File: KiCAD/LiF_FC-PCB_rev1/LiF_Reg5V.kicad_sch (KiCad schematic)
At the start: 21 parts, among them U3 TPS55285VALR

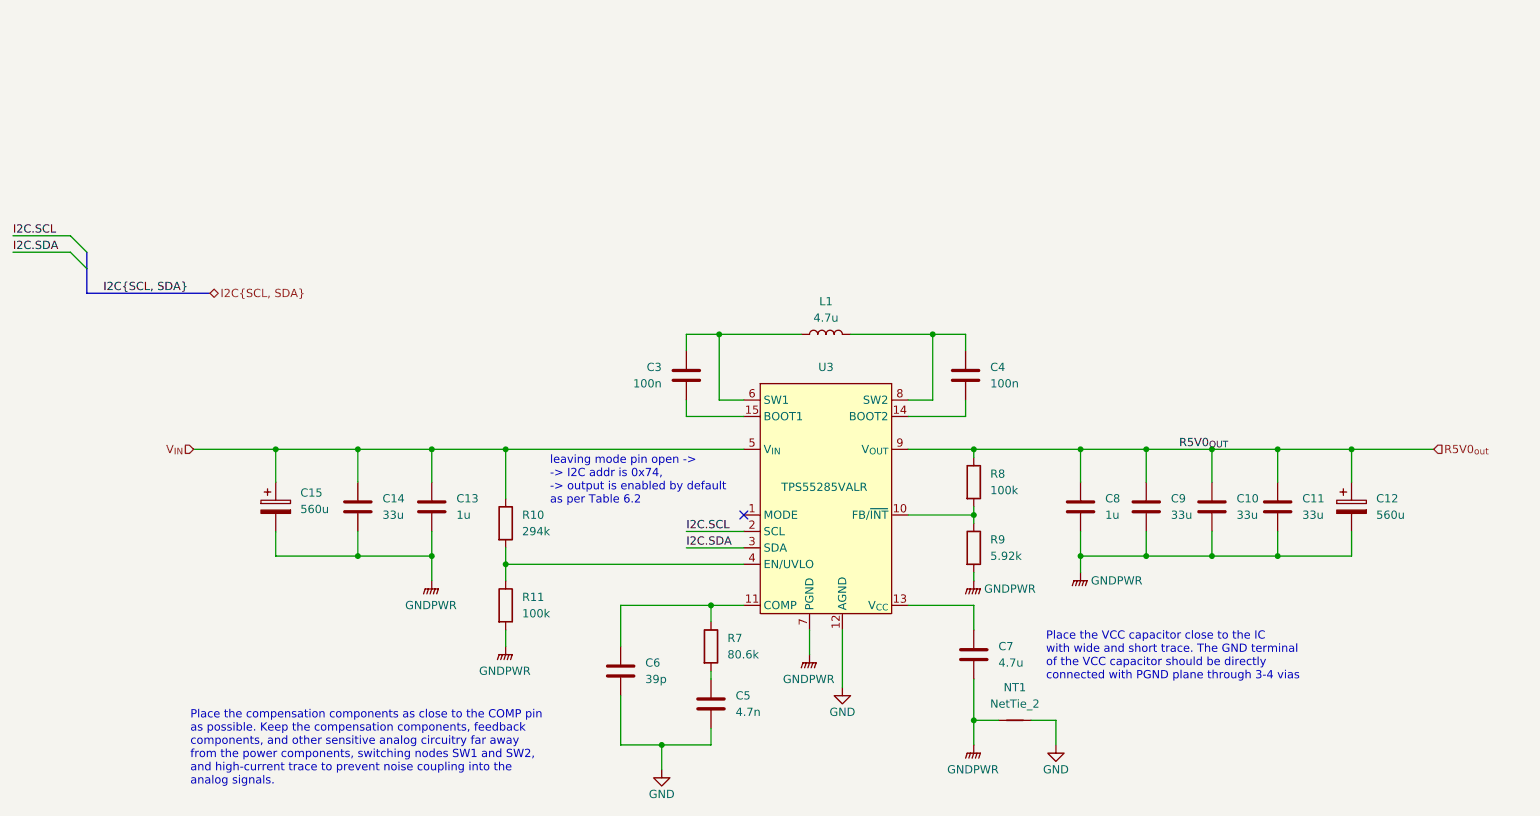
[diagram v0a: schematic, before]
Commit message: reverted 5V reg, reworked power distribution logic, swapped power OR-ing ICs
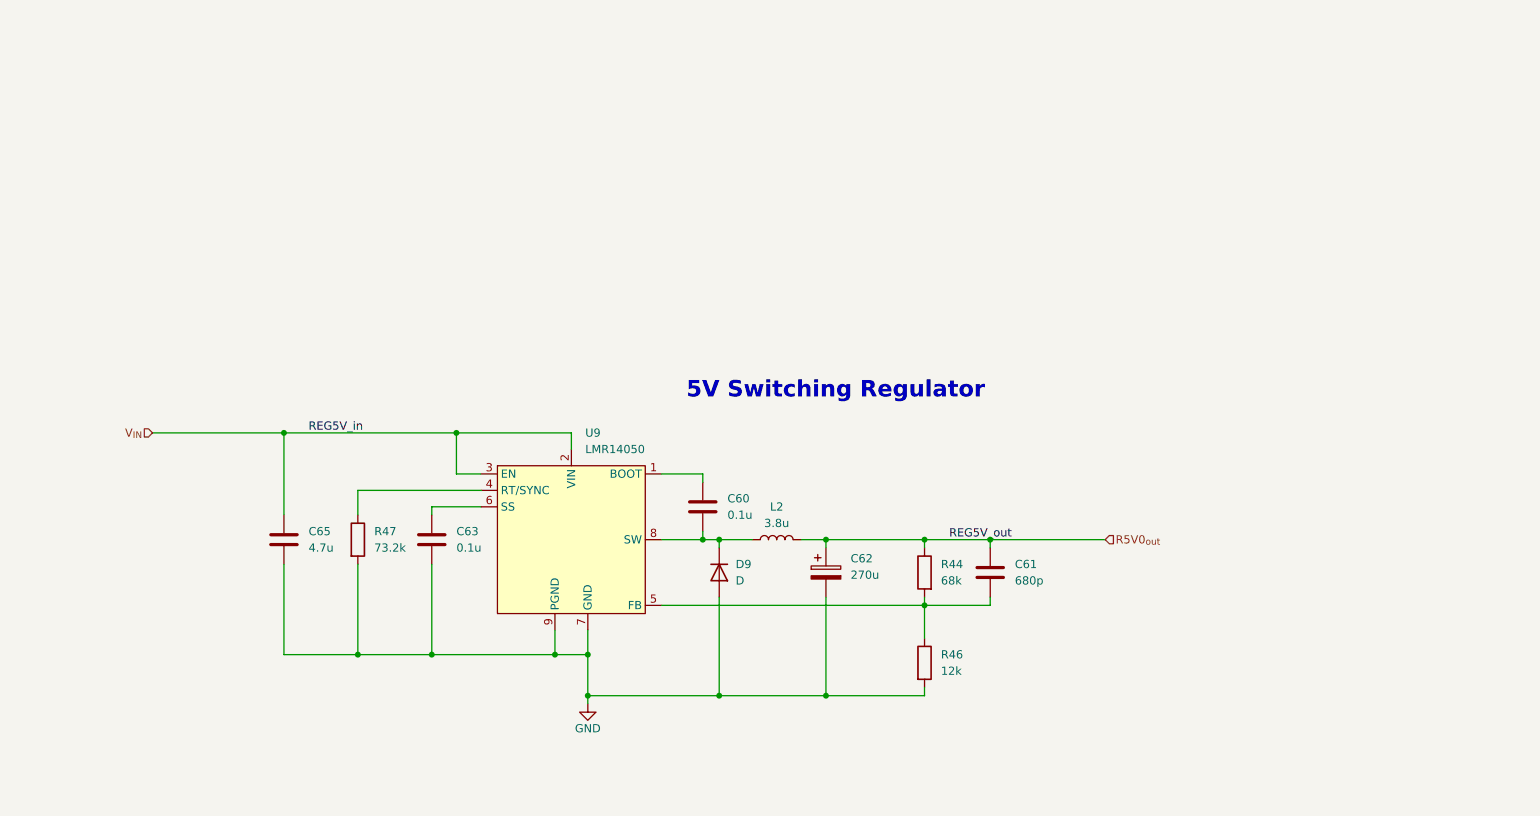
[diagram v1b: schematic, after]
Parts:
- removed C10, C11, C14, C9: 33u, symbol Device:C
- removed C12, C15: 560u, symbol Device:C_Polarized
- removed C13, C8: 1u, symbol Device:C
- removed C3, C4: 100n, symbol Device:C
- removed C5: 4.7n, symbol Device:C
- removed C6: 39p, symbol Device:C
- removed C7: 4.7u, symbol Device:C
- removed L1: 4.7u, LiF_PCB_Footprints:IND_SPM10040T-4R7M, symbol Device:L
- removed NT1: NetTie_2, NetTie:NetTie-2_SMD_Pad0.5mm, symbol Device:NetTie_2
- removed R10: 294k, symbol Device:R
- removed R11, R8: 100k, symbol Device:R
- removed R7: 80.6k, symbol Device:R
- removed R9: 5.92k, symbol Device:R
- removed U3: TPS55285VALR, LiF_PCB_Footprints:WQFN-HR-15, symbol LiF_PCB_Symbols:TPS55285VALR
- added C60, C63: 0.1u, Capacitor_SMD:C_0805_2012Metric, symbol Device:C
- added C61: 680p, Capacitor_SMD:C_0805_2012Metric, symbol Device:C
- added C62: 270u, Capacitor_SMD:CP_Elec_6.3x9.9, symbol Device:C_Polarized
- added C65: 4.7u, Capacitor_SMD:C_0805_2012Metric, symbol Device:C
- added D9: D, Diode_SMD:D_PowerDI-5, symbol Device:D
- added L2: 3.8u, MatsLibrary:IND_BOURNS_SRU1038, symbol Device:L
- added R44: 68k, Resistor_SMD:R_0805_2012Metric, symbol Device:R
- added R46: 12k, Resistor_SMD:R_0805_2012Metric, symbol Device:R
- added R47: 73.2k, Resistor_SMD:R_0805_2012Metric, symbol Device:R
- added U9: LMR14050, Package_SO:Texas_R-PDSO-G8_EP2.95x4.9mm_Mask2.4x3.1mm, symbol LiF_PCB_Symbols:LMR14050SDDAR
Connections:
- net GND: now also C62.2, C63.2, C65.2, D9.2 (A), R46.2, R47.2, U9.7 (GND), U9.9 (PGND)
- net R5V0_{out}: now also C61.1, C62.1, L2.2, R44.1
- net V_{IN}: now also C65.1, U9.2 (VIN), U9.3 (EN)
- new net: C60.2, D9.1 (K), L2.1, U9.8 (SW)
- new net: C60.1, U9.1 (BOOT)
- new net: R47.1, U9.4 (RT/SYNC)
- new net: C61.2, R44.2, R46.1, U9.5 (FB)
- new net: C63.1, U9.6 (SS)
- no-connect marks 1 -> 0
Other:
- note added: "5V Switching Regulator"
- note removed: "Place the VCC capacitor close to the IC with wide and short trace. The GND terminal of the VCC capacitor should be directly connected with PGND plane through 3-4 vias"
- note removed: "Place the compensation components as close to the COMP pin as possible. Keep the compensation components, feedback components, and other sensitive analog circuitry far away from the power components, switching nodes SW1 and SW2, and high-current trace to prevent noise coupling into the analog signals."
- note removed: "leaving mode pin open -> -> I2C addr is 0x74, -> output is enabled by default as per Table 6.2"

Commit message: Finished schematics, mostly. Only MCU sheet left. Doing component sourcing
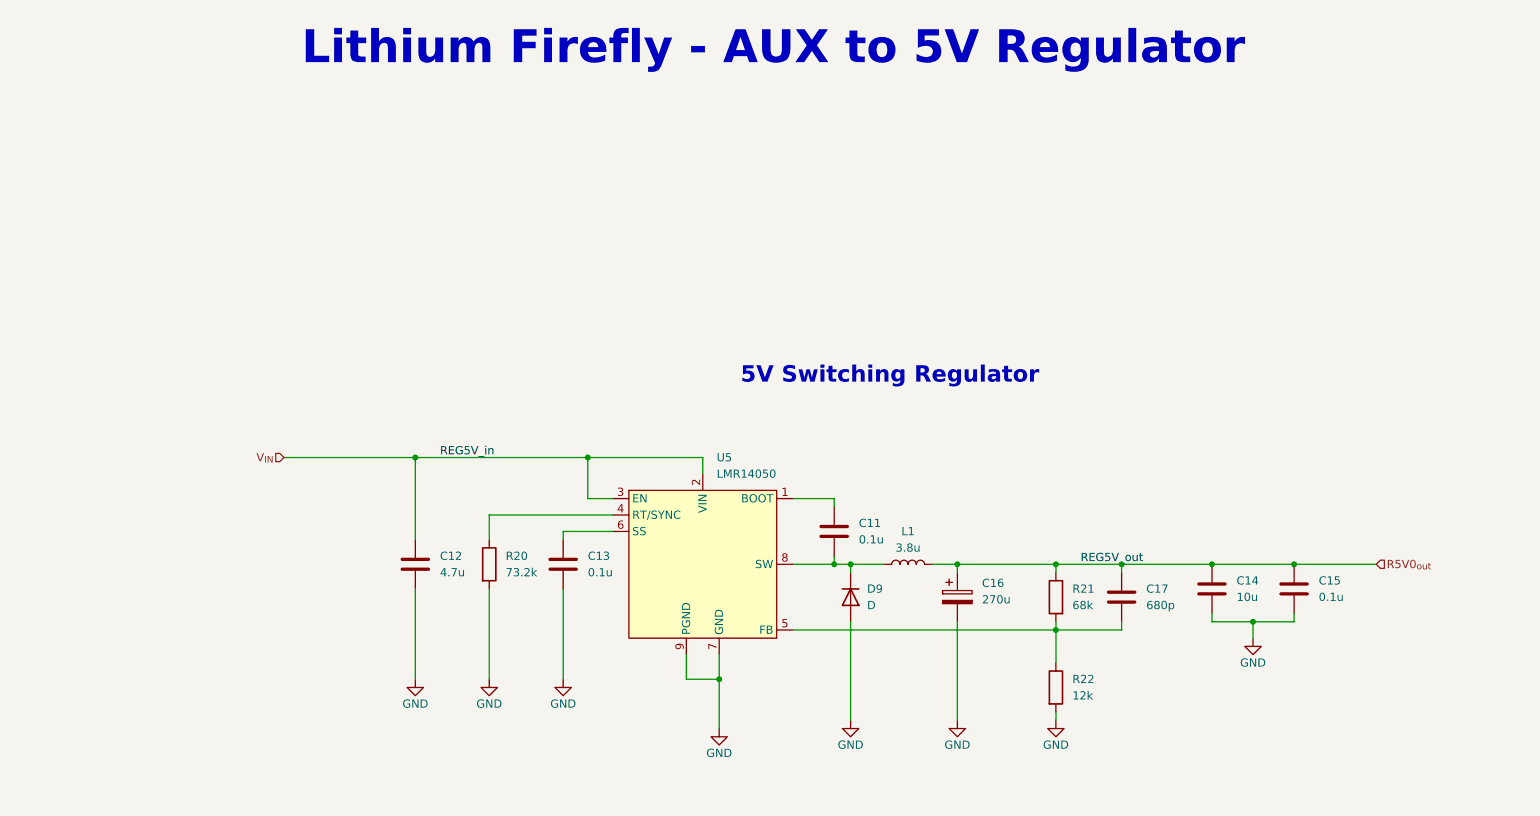
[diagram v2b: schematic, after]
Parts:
- added C14: 10u, Capacitor_SMD:C_0805_2012Metric, symbol Device:C
- added C15: 0.1u, Capacitor_SMD:C_0805_2012Metric, symbol Device:C
- C11: renamed from C60; DKPN (none) -> 490-12005-1-ND; PN (none) -> GRM21BR72A104KAC4L
- C12: renamed from C65; DK# 490-10751-1-ND -> (none); DKPN (none) -> 490-10751-1-ND; PN (none) -> GRM21BR61H475KE51L
- C13: renamed from C63; DKPN (none) -> 490-12005-1-ND; PN (none) -> GRM21BR72A104KAC4L
- C16: renamed from C62; DKPN (none) -> 732-6398-1-ND; PN (none) -> 875105144009
- C17: renamed from C61; DKPN (none) -> 490-10751-1-ND; PN (none) -> GRM21BR61H475KE51L
- D9: footprint Diode_SMD:D_PowerDI-5 -> Diode_SMD:D_SMB; DK# PDS760DICT-ND -> (none); DKPN (none) -> 4786-GSK745BCT-ND; PN (none) -> GSK745B; Part# PDS760-13 -> (none)
- L1: renamed from L2; footprint MatsLibrary:IND_BOURNS_SRU1038 -> LiF_PCB_Footprints:IND_BOURNS_SRU1038; DK# 308-1610-1-ND -> (none); DKPN (none) -> SRU1038-3R8YCT-ND; PN (none) -> SRU1038-3R8Y; Part# CDEP147NP-8R0MC-125 -> (none)
- renumbered R47 to R20, R44 to R21, R46 to R22, U9 to U5
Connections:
- net GND: now also C14.2, C15.2
- net R5V0_{out}: now also C14.1, C15.1
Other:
- note added: "Lithium Firefly - AUX to 5V Regulator"
- company: (none) -> Lithium Firefly Team
- moved on the sheet: C11, C12, C13, C16, C17, D9, L1, R20, R21, R22, U5

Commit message: fixing ERC bugs on schematic. Only MCU left
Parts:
- added TP10: R5V0, TestPoint:TestPoint_Bridge_Pitch2.54mm_Drill1.0mm, symbol Connector:TestPoint
- added TP11: GND, TestPoint:TestPoint_Bridge_Pitch2.54mm_Drill1.0mm, symbol Connector:TestPoint
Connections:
- net GND: now also TP11.1
- net R5V0_{out}: now also TP10.1

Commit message: Added MCU pinout, shanged shift registers to GPIO expanders to save pins on MCU
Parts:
- renumbered TP11 to TP10, TP10 to TP11
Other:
- title: (none) -> Lithium Firefly Custom FC/CC PCB
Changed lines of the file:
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@@
 	(paper "A4")
 	(title_block
+		(title "Lithium Firefly Custom FC/CC PCB")
+		(date "2026-07-11")
 		(rev "1")
 		(company "Lithium Firefly Team")
+		(comment 1 "Designed by MR")
 		(comment 2 "Verified by MR")
 	)
@@
 		(on_board yes)
 		(dnp no)
-		(property "Reference" "#PWR019"
+		(property "Reference" "#PWR024"
 			(at 217.17 118.11 0)
 			(effects
@@
 			(project "LiF_FC-PCB_rev1"
 				(path "/9e3e8da7-e506-46c9-90e5-307e4ad30d29/dbf56dc2-3990-4801-b0e0-f59d351af64c/18794d3c-1606-4c60-8412-e38df19bc4d8"
-					(reference "#PWR019")
+					(reference "#PWR024")
 					(unit 1)
 				)
@@
 		(on_board yes)
 		(dnp no)
-		(property "Reference" "#PWR022"
+		(property "Reference" "#PWR027"
 			(at 110.49 124.46 0)
 			(effects
@@
 			(project "LiF_FC-PCB_rev1"
 				(path "/9e3e8da7-e506-46c9-90e5-307e4ad30d29/dbf56dc2-3990-4801-b0e0-f59d351af64c/18794d3c-1606-4c60-8412-e38df19bc4d8"
-					(reference "#PWR022")
+					(reference "#PWR027")
 					(unit 1)
 				)
@@
 		(on_board yes)
 		(dnp no)
-		(property "Reference" "#PWR026"
+		(property "Reference" "#PWR031"
 			(at 134.62 132.08 0)
 			(effects
@@
 			(project "LiF_FC-PCB_rev1"
 				(path "/9e3e8da7-e506-46c9-90e5-307e4ad30d29/dbf56dc2-3990-4801-b0e0-f59d351af64c/18794d3c-1606-4c60-8412-e38df19bc4d8"
-					(reference "#PWR026")
+					(reference "#PWR031")
 					(unit 1)
 				)
@@
 		(on_board yes)
 		(dnp no)
-		(property "Reference" "TP11"
+		(property "Reference" "TP10"
 			(at 210.058 85.598 0)
 			(effects
@@
 			(project "LiF_FC-PCB_rev1"
 				(path "/9e3e8da7-e506-46c9-90e5-307e4ad30d29/dbf56dc2-3990-4801-b0e0-f59d351af64c/18794d3c-1606-4c60-8412-e38df19bc4d8"
-					(reference "TP11")
+					(reference "TP10")
 					(unit 1)
 				)
@@
 		(on_board yes)
 		(dnp no)
-		(property "Reference" "#PWR020"
+		(property "Reference" "#PWR025"
 			(at 87.63 124.46 0)
 			(effects
@@
 			(project "LiF_FC-PCB_rev1"
 				(path "/9e3e8da7-e506-46c9-90e5-307e4ad30d29/dbf56dc2-3990-4801-b0e0-f59d351af64c/18794d3c-1606-4c60-8412-e38df19bc4d8"
-					(reference "#PWR020")
+					(reference "#PWR025")
 					(unit 1)
 				)
@@
 		(on_board yes)
 		(dnp no)
-		(property "Reference" "#PWR024"
+		(property "Reference" "#PWR029"
 			(at 171.45 130.81 0)
 			(effects
@@
 			(project "LiF_FC-PCB_rev1"
 				(path "/9e3e8da7-e506-46c9-90e5-307e4ad30d29/dbf56dc2-3990-4801-b0e0-f59d351af64c/18794d3c-1606-4c60-8412-e38df19bc4d8"
-					(reference "#PWR024")
+					(reference "#PWR029")
 					(unit 1)
 				)
@@
 		(on_board yes)
 		(dnp no)
-		(property "Reference" "#PWR023"
+		(property "Reference" "#PWR028"
 			(at 154.94 130.81 0)
 			(effects
@@
 			(project "LiF_FC-PCB_rev1"
 				(path "/9e3e8da7-e506-46c9-90e5-307e4ad30d29/dbf56dc2-3990-4801-b0e0-f59d351af64c/18794d3c-1606-4c60-8412-e38df19bc4d8"
-					(reference "#PWR023")
+					(reference "#PWR028")
 					(unit 1)
 				)
@@
 		(on_board yes)
 		(dnp no)
-		(property "Reference" "#PWR0111"
+		(property "Reference" "#PWR023"
 			(at 208.28 97.79 0)
 			(effects
@@
 			(project "LiF_FC-PCB_rev1"
 				(path "/9e3e8da7-e506-46c9-90e5-307e4ad30d29/dbf56dc2-3990-4801-b0e0-f59d351af64c/18794d3c-1606-4c60-8412-e38df19bc4d8"
-					(reference "#PWR0111")
+					(reference "#PWR023")
 					(unit 1)
 				)
@@
 		(on_board yes)
 		(dnp no)
-		(property "Reference" "TP10"
+		(property "Reference" "TP11"
 			(at 219.71 86.8679 0)
 			(effects
@@
 			(project "LiF_FC-PCB_rev1"
 				(path "/9e3e8da7-e506-46c9-90e5-307e4ad30d29/dbf56dc2-3990-4801-b0e0-f59d351af64c/18794d3c-1606-4c60-8412-e38df19bc4d8"
-					(reference "TP10")
+					(reference "TP11")
 					(unit 1)
 				)
@@
 		(on_board yes)
 		(dnp no)
-		(property "Reference" "#PWR021"
+		(property "Reference" "#PWR026"
 			(at 99.06 124.46 0)
 			(effects
@@
 			(project "LiF_FC-PCB_rev1"
 				(path "/9e3e8da7-e506-46c9-90e5-307e4ad30d29/dbf56dc2-3990-4801-b0e0-f59d351af64c/18794d3c-1606-4c60-8412-e38df19bc4d8"
-					(reference "#PWR021")
+					(reference "#PWR026")
 					(unit 1)
 				)
@@
 		(on_board yes)
 		(dnp no)
-		(property "Reference" "#PWR025"
+		(property "Reference" "#PWR030"
 			(at 186.69 130.81 0)
 			(effects
@@
 			(project "LiF_FC-PCB_rev1"
 				(path "/9e3e8da7-e506-46c9-90e5-307e4ad30d29/dbf56dc2-3990-4801-b0e0-f59d351af64c/18794d3c-1606-4c60-8412-e38df19bc4d8"
-					(reference "#PWR025")
+					(reference "#PWR030")
 					(unit 1)
 				)

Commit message: set up board configuration and started routing PCB
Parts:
- TP10, TP11: footprint TestPoint:TestPoint_Bridge_Pitch2.54mm_Drill1.0mm -> TestPoint:TestPoint_Loop_D1.80mm_Drill1.0mm_Beaded
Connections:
- net SW: now reaches C11.2, D9.1 (K), L1.1, U5.8 (SW)
- net Boot: now reaches C11.1, U5.1 (BOOT)
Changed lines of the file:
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@@
+		)
+	)
+	(label "SW"
+		(at 147.32 100.33 0)
+		(effects
+			(font
+				(size 1.27 1.27)
+			)
+			(justify left bottom)
+		)
+	)
+	(label "Boot"
+		(at 147.32 90.17 0)
+		(effects
+			(font
+				(size 1.27 1.27)
+			)
+			(justify left bottom)
 		)
 	)
@@
 			)
 		)
-		(property "Footprint" "TestPoint:TestPoint_Bridge_Pitch2.54mm_Drill1.0mm"
+		(property "Footprint" "TestPoint:TestPoint_Loop_D1.80mm_Drill1.0mm_Beaded"
 			(at 213.36 90.17 0)
 			(effects
@@
 			)
 		)
-		(property "Footprint" "TestPoint:TestPoint_Bridge_Pitch2.54mm_Drill1.0mm"
+		(property "Footprint" "TestPoint:TestPoint_Loop_D1.80mm_Drill1.0mm_Beaded"
 			(at 222.25 91.44 0)
 			(effects
